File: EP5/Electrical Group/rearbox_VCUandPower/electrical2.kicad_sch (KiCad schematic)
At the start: 28 parts, among them IC6 LMR50410Y3FQDBVRQ1, J25 rear_connector

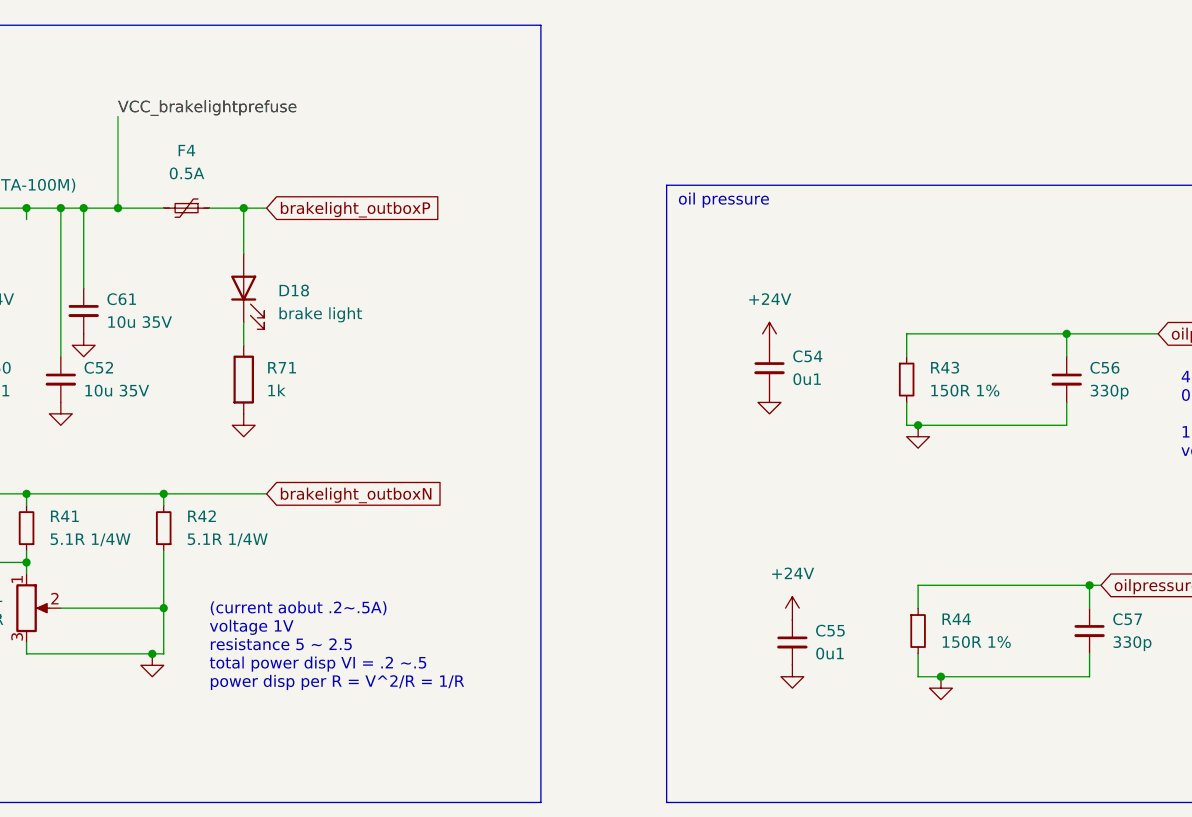
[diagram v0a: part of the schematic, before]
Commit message: add rearbox_VCUandPower to EP5
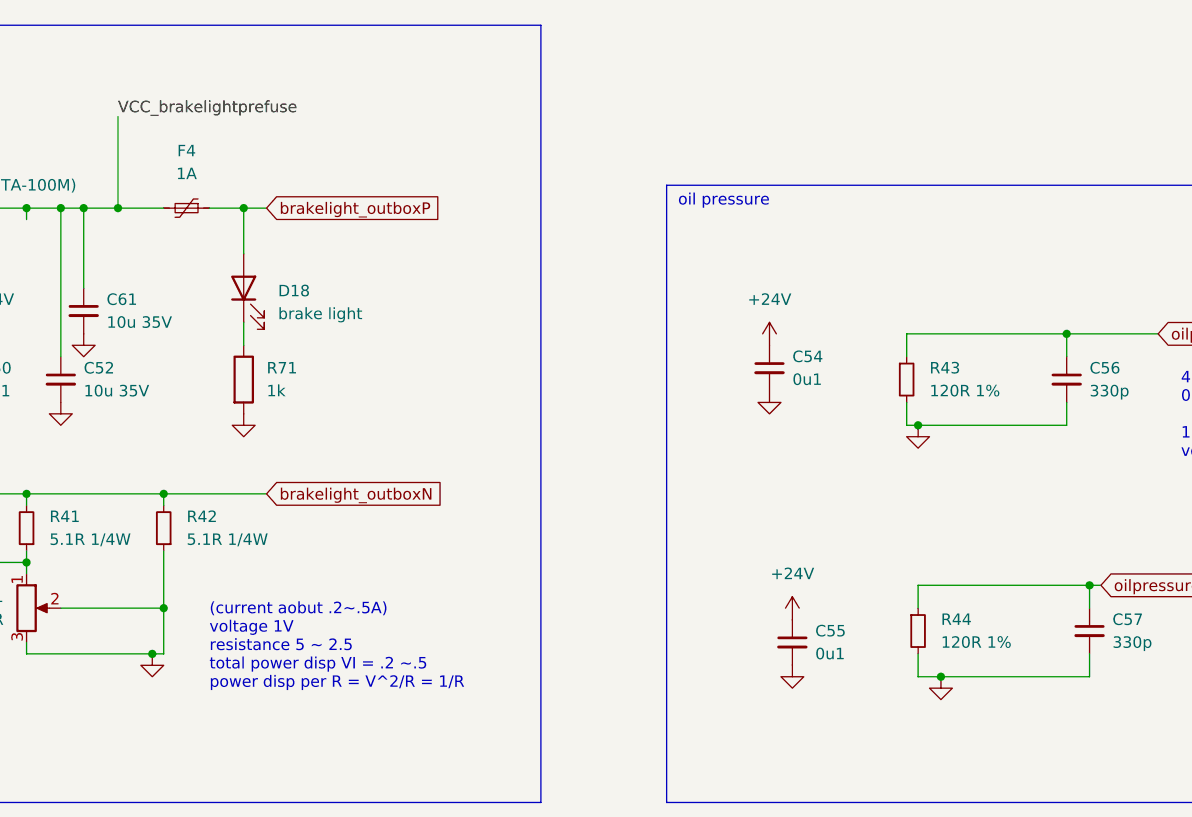
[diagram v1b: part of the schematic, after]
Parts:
- F4: value 0.5A -> 1A
- R43, R44: value 150R 1% -> 120R 1%
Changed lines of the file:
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@@
 		(rev "1.0")
 		(company "NTURacing")
-		(comment 1 "郭哲明")
+		(comment 1 "郭哲明 Jack Kuo")
 		(comment 2 "Electrical group")
 	)
@@
 			)
 		)
-		(property "Description" ""
+		(property "Description" "Unpolarized capacitor, small symbol"
 			(at 194.31 60.96 0)
 			(effects
@@
 			)
 		)
-		(property "Description" ""
+		(property "Description" "Power symbol creates a global label with name \"+24V\""
 			(at 104.14 168.91 0)
 			(effects
@@
 			)
 		)
-		(property "Description" ""
+		(property "Description" "Unpolarized capacitor, small symbol"
 			(at 82.55 60.96 0)
 			(effects
@@
 			)
 		)
-		(property "Value" "150R 1%"
+		(property "Value" "120R 1%"
 			(at 180.34 90.1699 0)
 			(effects
@@
 			)
 		)
-		(property "Description" ""
+		(property "Description" "Resistor, small symbol"
 			(at 177.8 88.9 0)
 			(effects
@@
 			)
 		)
-		(property "Description" ""
+		(property "Description" "Power symbol creates a global label with name \"GND\" , ground"
 			(at 85.09 55.88 0)
 			(effects
@@
 			)
 		)
-		(property "Description" ""
+		(property "Description" "Unpolarized capacitor, small symbol"
 			(at 71.12 60.96 0)
 			(effects
@@
 			)
 		)
-		(property "Description" ""
+		(property "Description" "Power symbol creates a global label with name \"+24V\""
 			(at 161.29 57.15 0)
 			(effects
@@
 			)
 		)
-		(property "Description" ""
+		(property "Description" "Unpolarized capacitor, small symbol"
 			(at 85.09 53.34 0)
 			(effects
@@
 			)
 		)
-		(property "Description" ""
+		(property "Description" "Resistor"
 			(at 66.04 55.88 0)
 			(effects
@@
 			)
 		)
-		(property "Description" ""
+		(property "Description" "Unpolarized capacitor, small symbol"
 			(at 22.86 87.63 0)
 			(effects
@@
 			)
 		)
-		(property "Description" ""
+		(property "Description" "Diode, small symbol"
 			(at 101.6 179.07 0)
 			(effects
@@
 			)
 		)
-		(property "Description" ""
+		(property "Description" "Power symbol creates a global label with name \"GND\" , ground"
 			(at 180.34 93.98 0)
 			(effects
@@
 			)
 		)
-		(property "Description" ""
+		(property "Description" "Potentiometer"
 			(at 78.74 86.36 0)
 			(effects
@@
 			)
 		)
-		(property "Description" ""
+		(property "Description" "Power symbol creates a global label with name \"+3V3\""
 			(at 66.04 120.65 0)
 			(effects
@@
 			)
 		)
-		(property "Description" ""
+		(property "Description" "Inductor, small symbol"
 			(at 71.12 41.91 0)
 			(effects
@@
 			)
 		)
-		(property "Description" ""
+		(property "Description" "Power symbol creates a global label with name \"GND\" , ground"
 			(at 39.37 90.17 0)
 			(effects
@@
 			)
 		)
-		(property "Description" ""
+		(property "Description" "Polarized capacitor, small symbol"
 			(at 39.37 87.63 0)
 			(effects
@@
 			)
 		)
-		(property "Description" ""
+		(property "Description" "Resistor, small symbol"
 			(at 93.98 77.47 0)
 			(effects
@@
 			)
 		)
-		(property "Value" "150R 1%"
+		(property "Value" "120R 1%"
 			(at 179.07 62.2299 0)
 			(effects
@@
 			)
 		)
-		(property "Description" ""
+		(property "Description" "Resistor, small symbol"
 			(at 176.53 60.96 0)
 			(effects
@@
 			)
 		)
-		(property "Description" ""
+		(property "Description" "Power symbol creates a global label with name \"+3V3\""
 			(at 102.87 158.75 0)
 			(effects
@@
 			)
 		)
-		(property "Description" ""
+		(property "Description" "Power symbol creates a global label with name \"GND\" , ground"
 			(at 21.59 44.45 0)
 			(effects
@@
 			)
 		)
-		(property "Description" ""
+		(property "Description" "Unpolarized capacitor, small symbol"
 			(at 102.87 123.19 0)
 			(effects
@@
 			)
 		)
-		(property "Description" ""
+		(property "Description" "Power symbol creates a global label with name \"GND\" , ground"
 			(at 22.86 90.17 0)
 			(effects
@@
 			)
 		)
-		(property "Description" ""
+		(property "Description" "Unpolarized capacitor, small symbol"
 			(at 43.18 120.65 0)
 			(effects
@@
 			)
 		)
-		(property "Description" ""
+		(property "Description" "Resistor, small symbol"
 			(at 78.74 77.47 0)
 			(effects
@@
 			)
 		)
-		(property "Description" ""
+		(property "Description" "Unpolarized capacitor, small symbol"
 			(at 81.28 121.92 0)
 			(effects
@@
 			)
 		)
-		(property "Description" ""
+		(property "Description" "Power symbol creates a global label with name \"+3V3\""
 			(at 102.87 120.65 0)
 			(effects
@@
 			)
 		)
-		(property "Description" ""
+		(property "Description" "Power symbol creates a global label with name \"GND\" , ground"
 			(at 163.83 92.71 0)
 			(effects
@@
 			)
 		)
-		(property "Description" ""
+		(property "Description" "Power symbol creates a global label with name \"+24V\""
 			(at 39.37 85.09 0)
 			(effects
@@
 			)
 		)
-		(property "Description" ""
+		(property "Description" "Resistor"
 			(at 66.04 66.04 0)
 			(effects
@@
 			)
 		)
-		(property "Value" "0.5A"
+		(property "Value" "1A"
 			(at 96.52 38.1 90)
 			(effects
@@
 			)
 		)
-		(property "Description" ""
+		(property "Description" "Resettable fuse, polymeric positive temperature coefficient, small symbol"
 			(at 96.52 41.91 0)
 			(effects
@@
 			)
 		)
-		(property "Description" ""
+		(property "Description" "Power symbol creates a global label with name \"+24V\""
 			(at 163.83 87.63 0)
 			(effects
@@
 			)
 		)
-		(property "Description" ""
+		(property "Description" "Unpolarized capacitor, small symbol"
 			(at 66.04 123.19 0)
 			(effects
@@
 			)
 		)
-		(property "Description" ""
+		(property "Description" "Unpolarized capacitor, small symbol"
 			(at 161.29 59.69 0)
 			(effects
@@
 			)
 		)
-		(property "Description" ""
+		(property "Description" "Light emitting diode"
 			(at 102.87 50.8 0)
 			(effects
@@
 			)
 		)
-		(property "Description" ""
+		(property "Description" "Power symbol creates a global label with name \"GND\" , ground"
 			(at 82.55 63.5 0)
 			(effects
@@
 			)
 		)
-		(property "Description" ""
+		(property "Description" "Power symbol creates a global label with name \"GND\" , ground"
 			(at 97.79 151.13 0)
 			(effects
@@
 			)
 		)
-		(property "Description" ""
+		(property "Description" "Power symbol creates a global label with name \"GND\" , ground"
 			(at 92.71 91.44 0)
 			(effects
@@
 			)
 		)
-		(property "Description" ""
+		(property "Description" "Power symbol creates a global label with name \"GND\" , ground"
 			(at 161.29 62.23 0)
 			(effects
@@
 			)
 		)
-		(property "Description" ""
+		(property "Description" "Power symbol creates a global label with name \"GND\" , ground"
 			(at 102.87 64.77 0)
 			(effects
@@
 			)
 		)
-		(property "Description" ""
+		(property "Description" "Resistor"
 			(at 102.87 60.96 0)
 			(effects
@@
 			)
 		)
-		(property "Description" ""
+		(property "Description" "Unpolarized capacitor, small symbol"
 			(at 196.85 88.9 0)
 			(effects
@@
 			)
 		)
-		(property "Description" ""
+		(property "Description" "Power symbol creates a global label with name \"GND\" , ground"
 			(at 177.8 66.04 0)
 			(effects
@@
 			)
 		)
-		(property "Description" ""
+		(property "Description" "Generic connector, single row, 01x16, script generated (kicad-library-utils/schlib/autogen/connector/)"
 			(at 72.39 163.83 0)
 			(effects
@@
 			)
 		)
-		(property "Description" ""
+		(property "Description" "Power symbol creates a global label with name \"+24V\""
 			(at 74.93 57.15 0)
 			(effects
@@
 			)
 		)
-		(property "Description" ""
+		(property "Description" "Power symbol creates a global label with name \"GND\" , ground"
 			(at 43.18 123.19 0)
 			(effects
@@
 			)
 		)
-		(property "Description" ""
+		(property "Description" "Unpolarized capacitor, small symbol"
 			(at 21.59 34.29 0)
 			(effects
@@
 			)
 		)
-		(property "Description" ""
+		(property "Description" "Power symbol creates a global label with name \"GND\" , ground"
 			(at 102.87 125.73 0)
 			(effects
@@
 			)
 		)
-		(property "Description" ""
+		(property "Description" "LMR50410Y3FQDBVRQ1"
 			(at 31.75 41.91 0)
 			(effects
@@
 			)
 		)
-		(property "Description" ""
+		(property "Description" "Power symbol creates a global label with name \"GND\" , ground"
 			(at 66.04 125.73 0)
 			(effects
@@
 			)
 		)
-		(property "Description" ""
+		(property "Description" "Unpolarized capacitor, small symbol"
 			(at 163.83 90.17 0)
 			(effects
@@
 			)
 		)
-		(property "Description" ""
+		(property "Description" "Power symbol creates a global label with name \"+24V\""
 			(at 22.86 85.09 0)
 			(effects
@@
 			)
 		)
-		(property "Description" ""
+		(property "Description" "Power symbol creates a global label with name \"GND\" , ground"
 			(at 81.28 124.46 0)
 			(effects
